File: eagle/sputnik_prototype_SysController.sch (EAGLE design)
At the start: 68 parts, among them U1 MEGA128-A, X1 CRYSTAL-ABRACON-ABM3-SMD

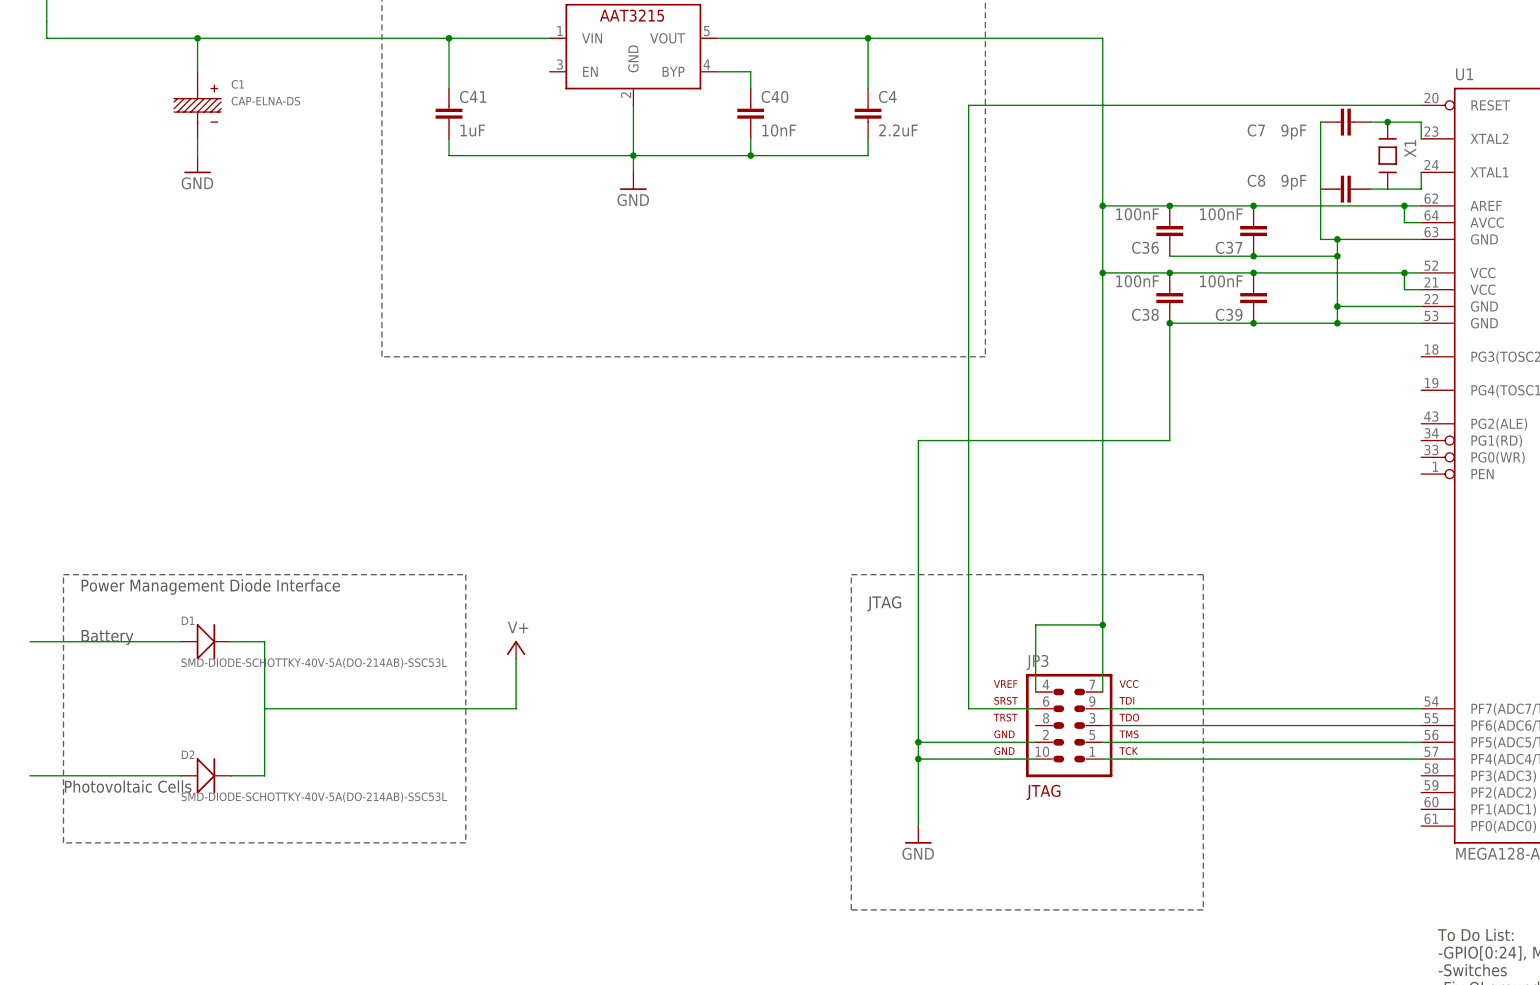
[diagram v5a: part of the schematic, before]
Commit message: added headers to power supply
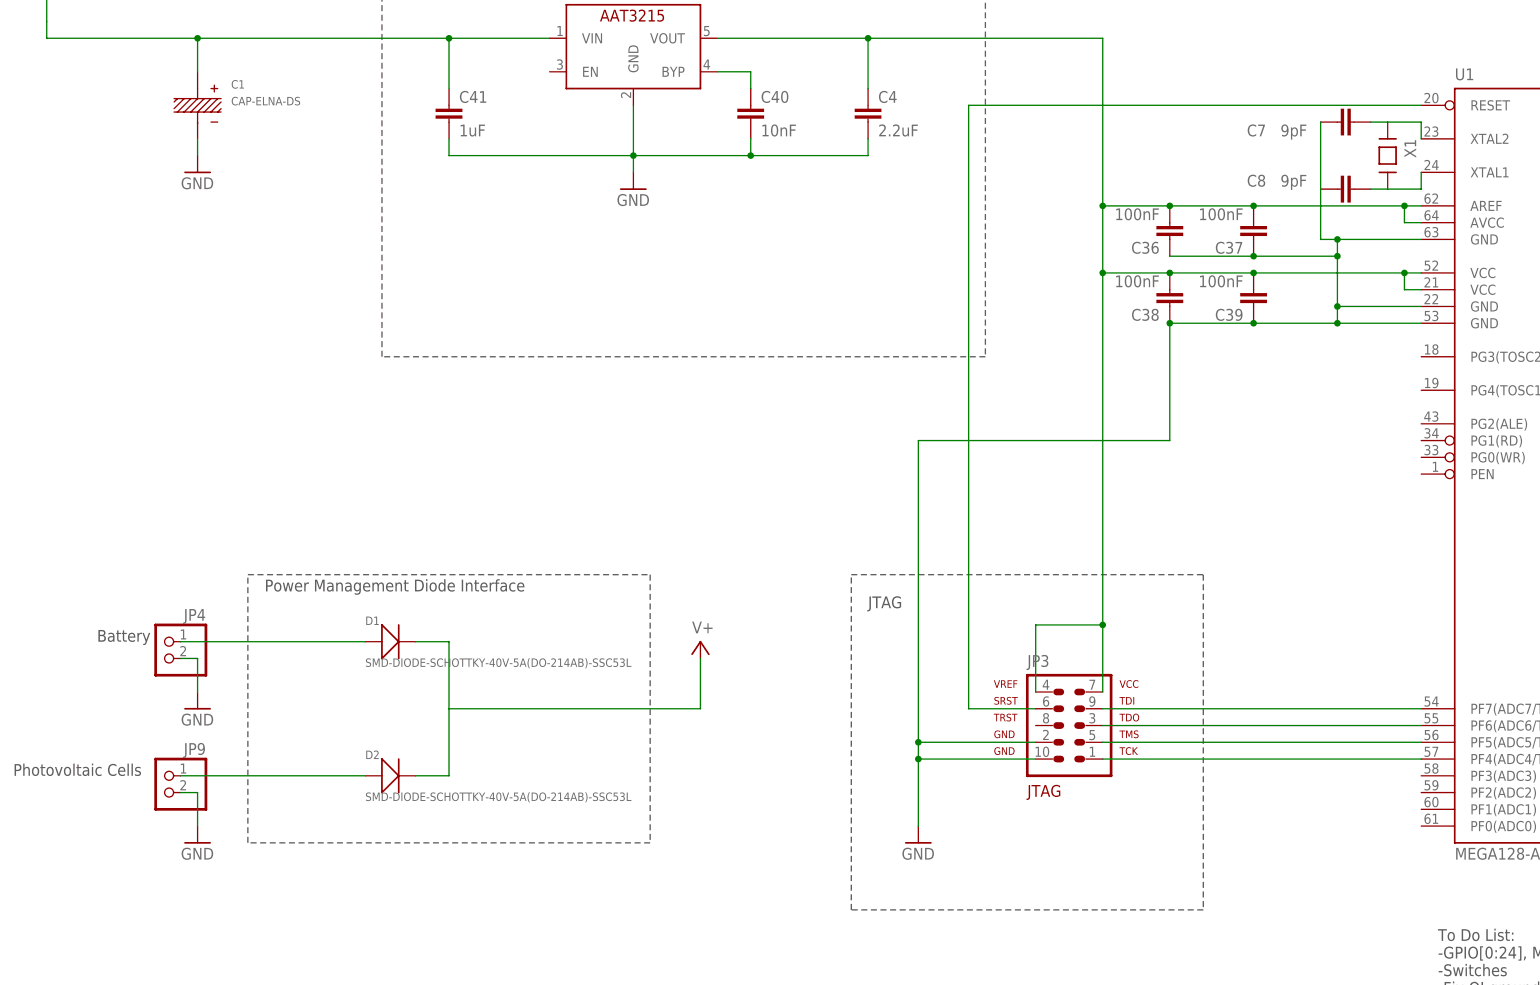
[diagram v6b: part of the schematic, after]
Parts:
- added JP4, JP9: (no value), psas_c3_team05:PINHD-1X2
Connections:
- net GND: now also JP4.2, JP9.2
- net N$25: now also JP4.1
- net N$26: now also JP9.1
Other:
- moved on the sheet: D1, D2
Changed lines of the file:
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@@
 <setting verticaltext="up"/>
 </settings>
-<grid distance="0.1" unitdist="inch" unit="inch" style="lines" multiple="1" display="yes" altdistance="0.01" altunitdist="inch" altunit="inch"/>
+<grid distance="0.1" unitdist="inch" unit="inch" style="lines" multiple="1" display="no" altdistance="0.01" altunitdist="inch" altunit="inch"/>
 <layers>
 <layer number="1" name="Top" color="4" fill="1" visible="no" active="no"/>
@@
 <part name="SUPPLY9" library="psas_c3_team05" deviceset="V+" device=""/>
 <part name="X1" library="crystal-abracon-abm3-smd" deviceset="CRYSTAL-ABRACON-ABM3-SMD" device=""/>
+<part name="JP4" library="psas_c3_team05" deviceset="PINHD-1X2" device=""/>
+<part name="JP9" library="psas_c3_team05" deviceset="PINHD-1X2" device=""/>
+<part name="GND12" library="psas_c3_team05" deviceset="GND" device=""/>
+<part name="GND13" library="psas_c3_team05" deviceset="GND" device=""/>
 </parts>
 <sheets>
@@
 <text x="370.84" y="101.6" size="1.778" layer="97">Optocouplers</text>
 <text x="137.16" y="297.18" size="1.778" layer="97">TODO: Replace this. We need a part that has a rad-hard analogue</text>
-<wire x1="76.2" y1="198.12" x2="137.16" y2="198.12" width="0.1524" layer="97" style="longdash"/>
-<wire x1="137.16" y1="198.12" x2="137.16" y2="157.48" width="0.1524" layer="97" style="longdash"/>
-<wire x1="137.16" y1="157.48" x2="76.2" y2="157.48" width="0.1524" layer="97" style="longdash"/>
-<wire x1="76.2" y1="157.48" x2="76.2" y2="198.12" width="0.1524" layer="97" style="longdash"/>
-<text x="78.74" y="195.58" size="1.778" layer="97">Power Management Diode Interface</text>
-<text x="78.74" y="187.96" size="1.778" layer="97">Battery</text>
-<text x="76.2" y="165.1" size="1.778" layer="97">Photovoltaic Cells</text>
+<wire x1="104.14" y1="198.12" x2="165.1" y2="198.12" width="0.1524" layer="97" style="longdash"/>
+<wire x1="165.1" y1="198.12" x2="165.1" y2="157.48" width="0.1524" layer="97" style="longdash"/>
+<wire x1="165.1" y1="157.48" x2="104.14" y2="157.48" width="0.1524" layer="97" style="longdash"/>
+<wire x1="104.14" y1="157.48" x2="104.14" y2="198.12" width="0.1524" layer="97" style="longdash"/>
+<text x="106.68" y="195.58" size="1.778" layer="97">Power Management Diode Interface</text>
+<text x="81.28" y="187.96" size="1.778" layer="97">Battery</text>
+<text x="68.58" y="167.64" size="1.778" layer="97">Photovoltaic Cells</text>
 </plain>
 <instances>
@@
 <instance part="C40" gate="CE" x="180.34" y="269.24"/>
 <instance part="C41" gate="CE" x="134.62" y="269.24"/>
-<instance part="D1" gate="G$1" x="97.79" y="187.96"/>
-<instance part="D2" gate="G$1" x="97.79" y="167.64"/>
-<instance part="SUPPLY9" gate="1" x="144.78" y="187.96"/>
+<instance part="D1" gate="G$1" x="125.73" y="187.96"/>
+<instance part="D2" gate="G$1" x="125.73" y="167.64"/>
+<instance part="SUPPLY9" gate="1" x="172.72" y="187.96"/>
 <instance part="X1" gate="G$1" x="276.86" y="261.62" rot="R270"/>
+<instance part="JP4" gate="G$1" x="91.44" y="185.42" rot="MR0"/>
+<instance part="JP9" gate="G$1" x="91.44" y="165.1" rot="MR0"/>
+<instance part="GND12" gate="1" x="96.52" y="157.48"/>
+<instance part="GND13" gate="1" x="96.52" y="177.8"/>
 </instances>
 <busses>
@@
 <junction x="180.34" y="261.62"/>
 </segment>
+<segment>
+<pinref part="JP9" gate="G$1" pin="2"/>
+<wire x1="93.98" y1="165.1" x2="96.52" y2="165.1" width="0.1524" layer="91"/>
+<wire x1="96.52" y1="165.1" x2="96.52" y2="160.02" width="0.1524" layer="91"/>
+<pinref part="GND12" gate="1" pin="GND"/>
+</segment>
+<segment>
+<pinref part="JP4" gate="G$1" pin="2"/>
+<wire x1="93.98" y1="185.42" x2="96.52" y2="185.42" width="0.1524" layer="91"/>
+<wire x1="96.52" y1="185.42" x2="96.52" y2="180.34" width="0.1524" layer="91"/>
+<pinref part="GND13" gate="1" pin="GND"/>
+</segment>
 </net>
 <net name="V+" class="0">
@@
 <segment>
 <pinref part="D1" gate="G$1" pin="-"/>
-<wire x1="101.6" y1="187.96" x2="106.68" y2="187.96" width="0.1524" layer="91"/>
-<wire x1="106.68" y1="187.96" x2="106.68" y2="177.8" width="0.1524" layer="91"/>
+<wire x1="129.54" y1="187.96" x2="134.62" y2="187.96" width="0.1524" layer="91"/>
+<wire x1="134.62" y1="187.96" x2="134.62" y2="177.8" width="0.1524" layer="91"/>
 <pinref part="D2" gate="G$1" pin="-"/>
-<wire x1="106.68" y1="177.8" x2="106.68" y2="167.64" width="0.1524" layer="91"/>
-<wire x1="106.68" y1="167.64" x2="101.6" y2="167.64" width="0.1524" layer="91"/>
-<wire x1="106.68" y1="177.8" x2="144.78" y2="177.8" width="0.1524" layer="91"/>
-<wire x1="144.78" y1="177.8" x2="144.78" y2="185.42" width="0.1524" layer="91"/>
+<wire x1="134.62" y1="177.8" x2="134.62" y2="167.64" width="0.1524" layer="91"/>
+<wire x1="134.62" y1="167.64" x2="129.54" y2="167.64" width="0.1524" layer="91"/>
+<wire x1="134.62" y1="177.8" x2="172.72" y2="177.8" width="0.1524" layer="91"/>
+<wire x1="172.72" y1="177.8" x2="172.72" y2="185.42" width="0.1524" layer="91"/>
 <pinref part="SUPPLY9" gate="1" pin="V+"/>
 </segment>
@@
 <net name="N$17" class="0">
 <segment>
-<pinref part="C7" gate="CE" pin="2"/>
 <pinref part="U1" gate="G$1" pin="XTAL2"/>
-<wire x1="274.32" y1="266.7" x2="276.86" y2="266.7" width="0.1524" layer="91"/>
-<wire x1="276.86" y1="266.7" x2="281.94" y2="266.7" width="0.1524" layer="91"/>
 <wire x1="281.94" y1="266.7" x2="281.94" y2="264.16" width="0.1524" layer="91"/>
 <pinref part="X1" gate="G$1" pin="P$1"/>
-<junction x="276.86" y="266.7"/>
+<pinref part="C7" gate="CE" pin="2"/>
+<wire x1="274.32" y1="266.7" x2="276.86" y2="266.7" width="0.1524" layer="91"/>
+<wire x1="281.94" y1="266.7" x2="276.86" y2="266.7" width="0.1524" layer="91"/>
 </segment>
 </net>
@@
 <segment>
 <pinref part="D1" gate="G$1" pin="+"/>
-<wire x1="93.98" y1="187.96" x2="71.12" y2="187.96" width="0.1524" layer="91"/>
+<wire x1="121.92" y1="187.96" x2="93.98" y2="187.96" width="0.1524" layer="91"/>
+<pinref part="JP4" gate="G$1" pin="1"/>
 </segment>
 </net>
@@
 <segment>
 <pinref part="D2" gate="G$1" pin="+"/>
-<wire x1="93.98" y1="167.64" x2="71.12" y2="167.64" width="0.1524" layer="91"/>
-</segment>
-</net>
+<wire x1="121.92" y1="167.64" x2="93.98" y2="167.64" width="0.1524" layer="91"/>
+<pinref part="JP9" gate="G$1" pin="1"/>
+</segment>
+</net>

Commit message: Clean up on system controller board. Added 40 pin connector, board outline, ground planes. Killed all old spurious signals. Removed unecessary connectors. Still need to find small power controllers to sequence power to other boards.
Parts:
- removed JP1, JP2, JP4, JP5, JP9: (no value), psas_c3_team05:PINHD-1X2
- removed JP6, JP7, JP8: (no value), psas_c3_team05:PINHD-2X10
- removed R13, R4, R6, R9: 390, rcl_custom:R-US_0603-B-NOSILK
- removed TP4, TP5: TPSPAD1-13, testpad:TPSPAD1-13
- added CF1: ORESAT-CONNECTOR-40PIN, oresat-eagle:ORESAT-CONNECTOR-40PIN
- added R12: 10k, rcl_custom:R-US_0603-B-NOSILK
- added TP1: TPSPAD1-13, testpad:TPSPAD1-13
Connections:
- removed net N$2: C36.2, C37.2, C38.2, C39.2, C4.1, JP3.4, JP3.7, U$8.VOUT, U1.AREF, U1.AVCC, U1.VCC, U1.VCC@1
- removed net N$21: R9.1, U$4.GND1
- removed net N$25: D1.+, JP4.1
- removed net N$26: D2.+, JP9.1
- removed net N$3: R13.1, U$3.GND1
- removed net N$7: R4.1, U$1.GND1
- removed net N$9: R6.1
- removed net PTA1/UART0_RX: R1.1
- removed net PTA2/UART1_TX: R10.1
- removed net PTA20/RESET: U1.(OC3A/AIN1)PE3
- removed net UART1_RX: JP5.1, R2.1, TP4.PP
- removed net UART1_TX: JP5.2, R5.1, TP5.PP
- new net +3V3: C2.2, C3.2, C36.2, C37.2, C38.2, C39.2, C4.1, JP3.4, JP3.7, U$2.VDD, U$4.VDD, U$8.VOUT, U1.AREF, U1.AVCC, U1.VCC, U1.VCC@1
- new net FC_UART_RX: CF1.19, CF1.20, R2.1
- new net FC_UART_TX: CF1.21, CF1.22, R5.1
- new net FC_UART_VCC: C5.2, CF1.17, CF1.18, U$1.VDD
- new net LGR_UART_RX: CF1.25, CF1.26, R1.1
- new net LGR_UART_TX: CF1.27, CF1.28, R10.1
- new net LGR_UART_VCC: C6.2, CF1.23, CF1.24, U$3.VDD
- new net N$22: R12.2, TP1.PP, U$8.EN
- new net VBUS: CF1.29, CF1.30, CF1.31, CF1.32, D1.+
- new net VSOL: CF1.33, CF1.34, CF1.35, CF1.36, D2.+
- net GND: now also CF1.37, CF1.38, CF1.39, CF1.40, U$1.GND1, U$3.GND1, U$4.GND1; no longer JP1.2, JP4.2, JP6.19, JP6.20, JP7.19, JP7.20, JP8.19, JP8.20, JP9.2, R13.2, R4.2, R6.2, R9.2
- net N$36: now also R12.1; no longer C1.+
- net PA0: no longer JP6.17, JP6.18
- net PA1: no longer JP6.15, JP6.16
- net PA2: no longer JP6.13, JP6.14
- net PA3: no longer JP6.11, JP6.12
- net PA4: no longer JP6.10, JP6.9
- net PA5: no longer JP6.7, JP6.8
- net PA6: no longer JP6.5, JP6.6
- net PA7: no longer JP6.3, JP6.4
- net PB0: no longer JP7.17, JP7.18
- net PB1: no longer JP7.15, JP7.16
- net PB2: no longer JP7.13, JP7.14
- net PB3: no longer JP7.11, JP7.12
- net PB4: no longer JP7.10, JP7.9
- net PB5: no longer JP7.7, JP7.8
- net PB6: no longer JP7.5, JP7.6
- net PB7: no longer JP7.3, JP7.4
- net PC0: no longer JP8.17, JP8.18
- net PC1: no longer JP8.15, JP8.16
- net PC2: no longer JP8.13, JP8.14
- net PC3: no longer JP8.11, JP8.12
- net PC4: no longer JP8.10, JP8.9
- net PC5: no longer JP8.7, JP8.8
- net PC6: no longer JP8.5, JP8.6
- net PC7: no longer JP8.3, JP8.4
- net SDA: now also CF1.15, CF1.16; no longer JP2.2
- net SDL: now also CF1.13, CF1.14; no longer JP2.1
- net V+: now also C1.+; no longer C2.2, C3.2, C5.2, C6.2, JP1.1, JP6.1, JP6.2, JP7.1, JP7.2, JP8.1, JP8.2, U$1.VDD, U$2.VDD, U$3.VDD, U$4.VDD
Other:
- note added: "Battery bus"
- note added: "Main Power Bus"
- note added: "Power Control for: 0. SPS/SBS (nuclear option) 1. LGR 2. FC 3. DxWiFi PA 4. ACS-RW 5. ACS-MAG 6. IMU 7. SDR-GPS 8. ADS-Sunsensors 9.ADS-Starfinder/Sunsensor"
- note added: "Solar bus"
- note removed: "Battery"
- note removed: "GPIO"
- note removed: "JTAG"
- note removed: "Low-gain Radio (KW0x)"
- note removed: "Optocouplers"
- note removed: "Payload interface"
- note removed: "Photovoltaic Cells"
- note removed: "Power Management Diode Interface"
- note removed: "Still need nuke pin here"
- note removed: "UART (WD)"
- note removed: "UART connection between KW0x and ATMega128 PTA1 = KW0x UART0 RX PTA2 = KW0x UART0 TX PE1 = ATMega128 UART0 TX PE0 = ATMega128 UART0 RX PE1 is connected to PTA1 PE0 is connected to PTA2"
- note removed: "control"
- note removed: "i2c"
- note removed: "power"
- moved on the sheet: C1, C2, C3, C4, C7, C8, D1, D2, JP3, R1, R10, R2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

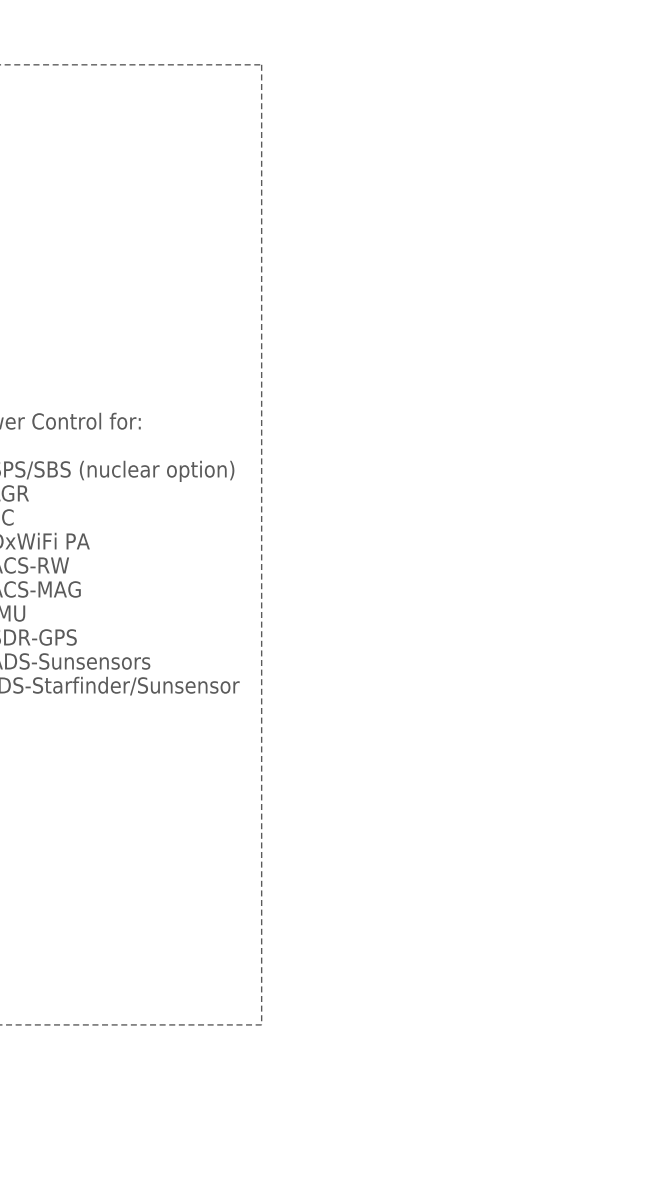
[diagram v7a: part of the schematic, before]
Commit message: Newest outline of SC board, added secondary connector because we're going to need it for the output.
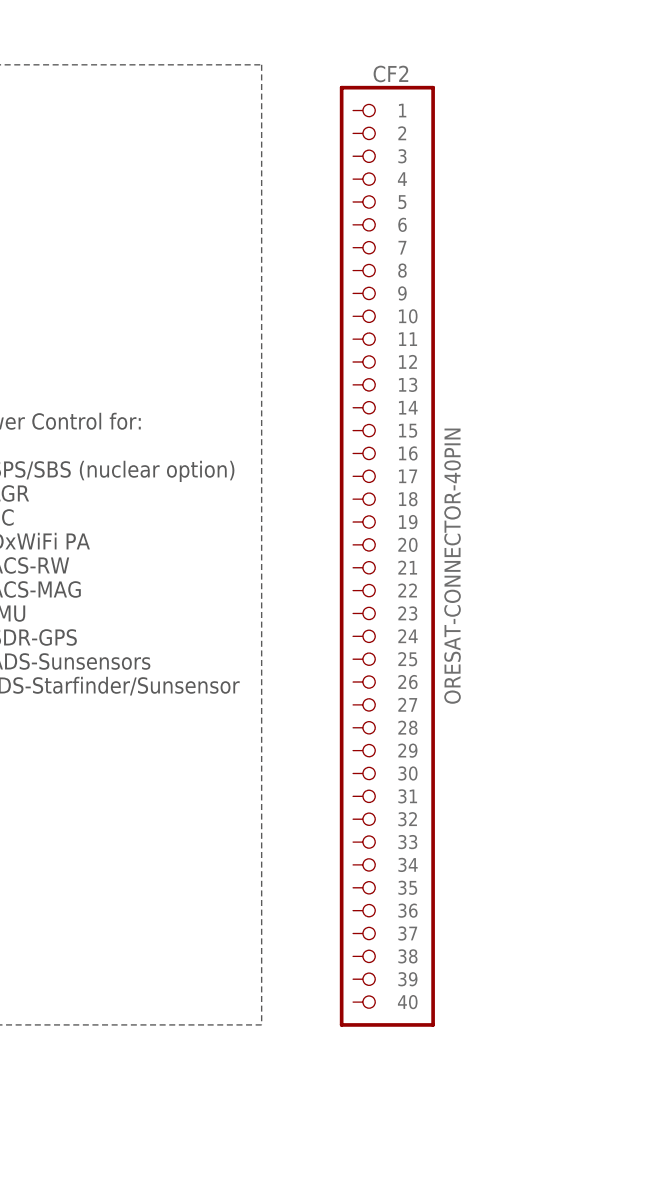
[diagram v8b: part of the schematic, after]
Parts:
- added CF2: ORESAT-CONNECTOR-40PIN, oresat-eagle:ORESAT-CONNECTOR-40PIN
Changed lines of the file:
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@@
 <setting verticaltext="up"/>
 </settings>
-<grid distance="0.05" unitdist="inch" unit="inch" style="lines" multiple="2" display="yes" altdistance="0.01" altunitdist="inch" altunit="inch"/>
+<grid distance="0.1" unitdist="inch" unit="inch" style="lines" multiple="1" display="no" altdistance="0.01" altunitdist="inch" altunit="inch"/>
 <layers>
 <layer number="1" name="Top" color="4" fill="1" visible="no" active="no"/>
@@
 <part name="+3V4" library="supply1" deviceset="+3V3" device=""/>
 <part name="+3V5" library="supply1" deviceset="+3V3" device=""/>
+<part name="CF2" library="oresat-eagle" deviceset="ORESAT-CONNECTOR-40PIN" device=""/>
 </parts>
 <sheets>
@@
 <instance part="+3V4" gate="G$1" x="375.92" y="109.22"/>
 <instance part="+3V5" gate="G$1" x="375.92" y="172.72"/>
+<instance part="CF2" gate="G$1" x="495.3" y="252.73" smashed="yes" rot="MR0">
+<attribute name="NAME" x="501.65" y="305.435" size="1.778" layer="95" rot="MR0"/>
+<attribute name="VALUE" x="505.46" y="236.22" size="1.778" layer="96" rot="MR90"/>
+</instance>
 </instances>
 <busses>
